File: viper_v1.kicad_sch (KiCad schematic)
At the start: 149 parts, among them J1 USB_B_Mini, J2 AVR-ISP-6, SW1 SW_RESET, SW10 KC_8, SW11 KC_9, SW12 KC_0, SW13 KC_MINS, SW14 KC_EQL, SW15 KC_BSPC, SW16 KC_TAB, SW17 KC_Q, SW18 KC_W, SW19 KC_E, SW2 KC_GRV, SW20 KC_R, SW21 KC_T, SW22 KC_Y, SW23 KC_U, SW24 KC_I, SW25 KC_O, SW26 KC_P, SW27 KC_LBRC, SW28 KC_RBRC, SW29 KC_BSLS, SW3 KC_1, SW30 KC_CAPS, SW31 KC_A, SW32 KC_S, SW33 KC_D, SW34 KC_F, SW35 KC_G, SW36 KC_H, SW37 KC_J, SW38 KC_K, SW39 KC_L, SW4 KC_2, SW40 KC_SCLN, SW41 KC_QUOT, SW42 KC_ENT, SW43 KC_LSFT, SW44 KC_Z, SW45 KC_X, SW46 KC_C, SW47 KC_V, SW48 KC_B, SW49 KC_N, SW5 KC_3, SW50 KC_M, SW51 KC_COMM, SW52 KC_DOT, SW53 KC_SLSH, SW54 KC_RSFT, SW55 KC_LEFT_GUI, SW56 KC_LEFT_ALT, SW57 KC_SPACE, SW58 KC_RIGHT_GUI, SW59 KC_RIGHT_ALT, SW6 KC_4, SW60 KC_BSPC, SW61 KC_BSPC, SW62 KC_BSPC, SW7 KC_5, SW8 KC_6, SW9 KC_7, U1 ATmega32U4-A, Y1 16MHz

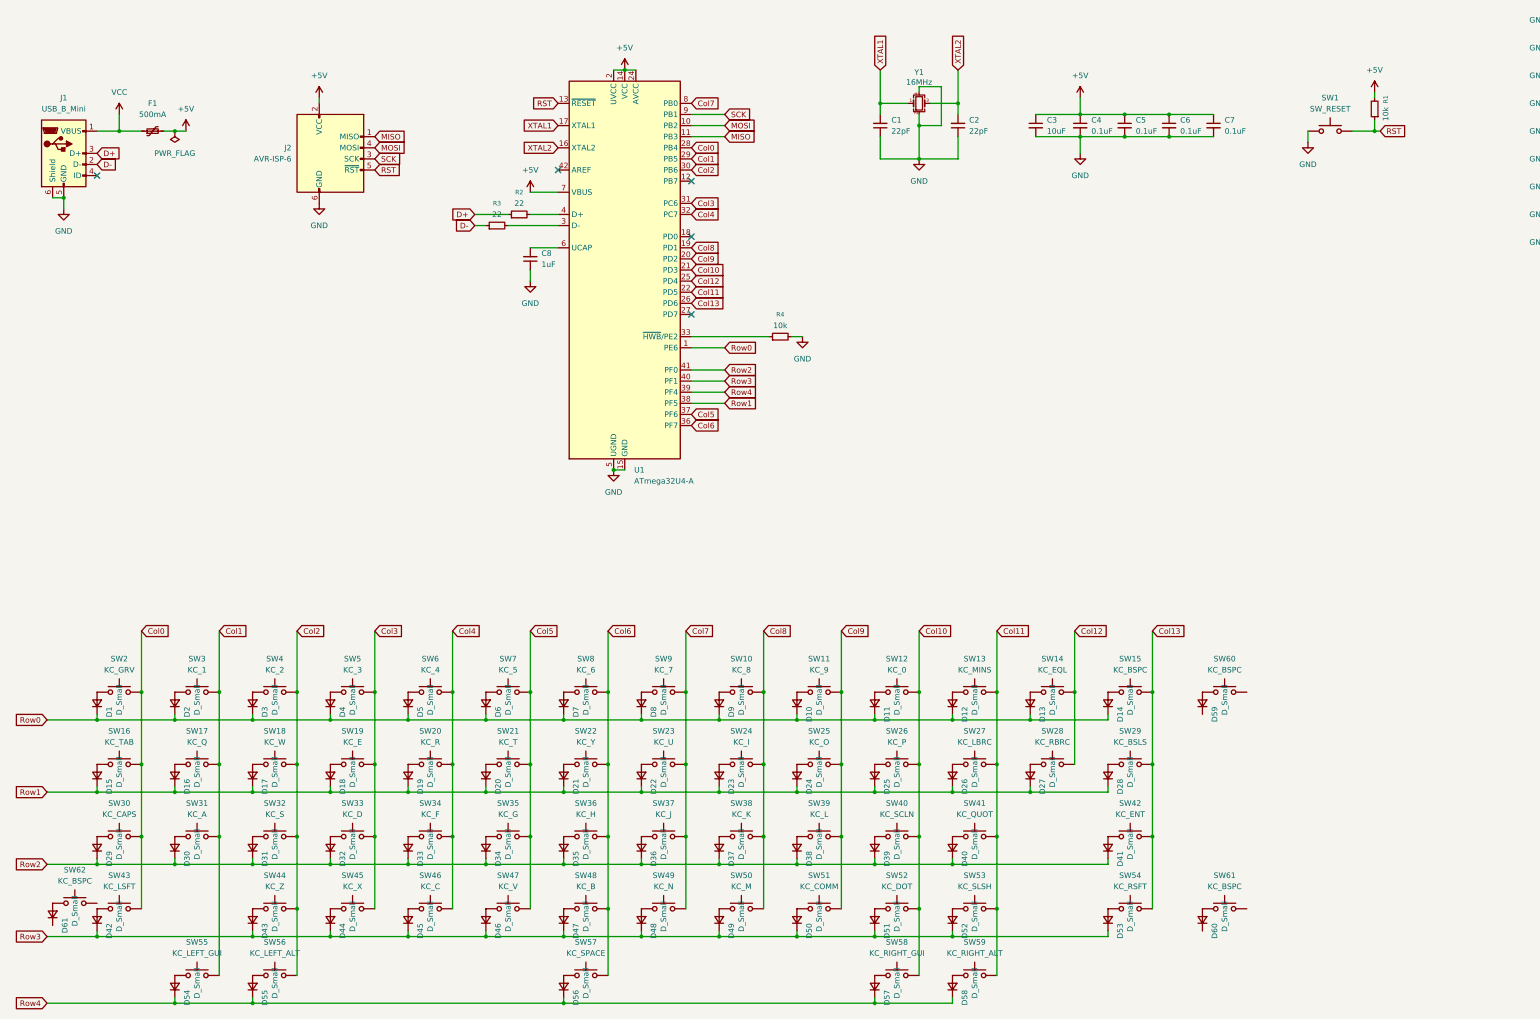
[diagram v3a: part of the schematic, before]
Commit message: Placed new footprints for iso enter, short shifts, stepped caps, fn & 2 more iso switches.
Added USBLC6-2SC6 for ESD protection
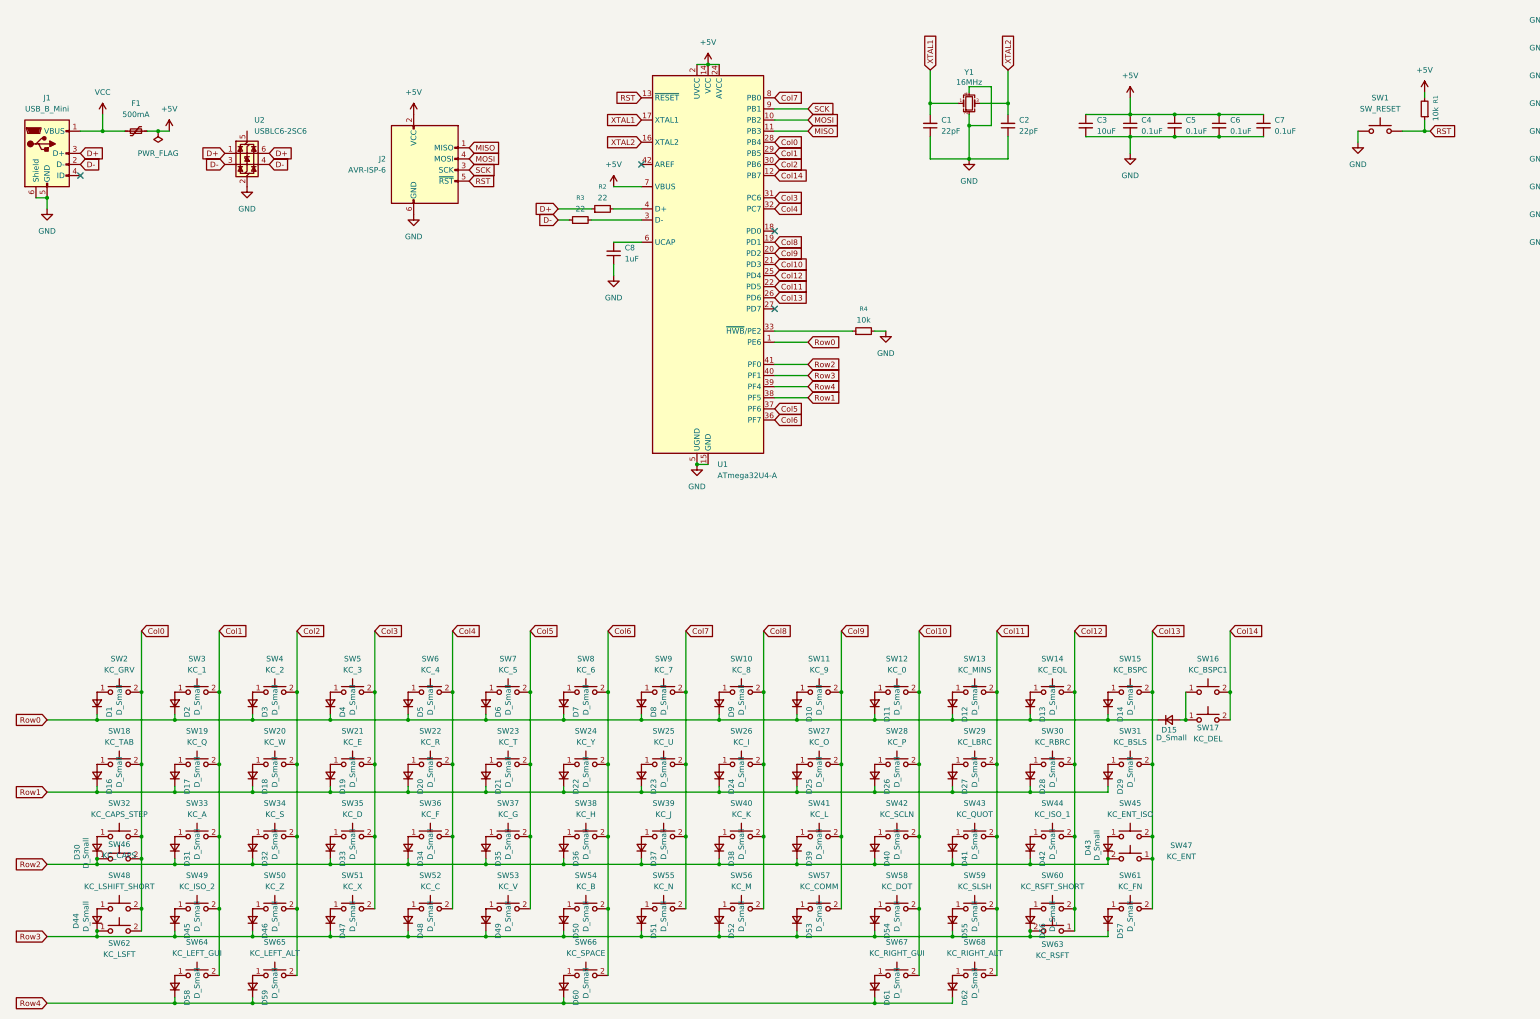
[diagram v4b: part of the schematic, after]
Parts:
- removed D60, D61: D_Small, Diode_SMD:D_SOD-123, symbol Device:D_Small
- added D42, D45, D56: D_Small, Diode_SMD:D_SOD-123, symbol Device:D_Small
- added SW44: KC_ISO_1, MX_Solderable:MX-Solderable-1U, symbol Switch:SW_Push
- added SW46: KC_CAPS, MX_Solderable:MX-Solderable-1.75U, symbol Switch:SW_Push
- added SW47: KC_ENT, MX_Solderable:MX-Solderable-2.25U-ReversedStabilizers, symbol Switch:SW_Push
- added SW49: KC_ISO_2, MX_Solderable:MX-Solderable-1U, symbol Switch:SW_Push
- added SW60: KC_RSFT_SHORT, MX_Solderable:MX-Solderable-1.75U, symbol Switch:SW_Push
- added SW63: KC_RSFT, MX_Solderable:MX-Solderable-2.75U-ReversedStabilizers, symbol Switch:SW_Push
- added U2: USBLC6-2SC6, Package_TO_SOT_SMD:SOT-23-6, symbol Power_Protection:USBLC6-2SC6
- SW16: renamed from SW60; value KC_BSPC -> KC_BSPC1; footprint MX_Solderable:MX-Solderable-2U -> MX_Solderable:MX-Solderable-1U
- SW17: renamed from SW61; value KC_BSPC -> KC_DEL; footprint MX_Solderable:MX-Solderable-2U -> MX_Solderable:MX-Solderable-1U
- SW32: renamed from SW30; value KC_CAPS -> KC_CAPS_STEP; footprint MX_Solderable:MX-Solderable-1.75U -> MX_Solderable:MX-Solderable-1.25U
- SW45: renamed from SW42; value KC_ENT -> KC_ENT_ISO; footprint MX_Solderable:MX-Solderable-2.25U-ReversedStabilizers -> MX_Solderable:MX-Solderable-2U-Vertical
- SW48: renamed from SW62; value KC_BSPC -> KC_LSHIFT_SHORT; footprint MX_Solderable:MX-Solderable-2U -> MX_Solderable:MX-Solderable-1.25U
- SW61: renamed from SW54; value KC_RSFT -> KC_FN; footprint MX_Solderable:MX-Solderable-2.75U-ReversedStabilizers -> MX_Solderable:MX-Solderable-1U
- renumbered D59 to D15, D15 to D16, D16 to D17, D17 to D18, D18 to D19, D19 to D20, D20 to D21, D21 to D22, D22 to D23, D23 to D24, D24 to D25, D25 to D26, D26 to D27, D27 to D28, D28 to D29, D29 to D30, D30 to D31, D31 to D32, D32 to D33, D33 to D34, D34 to D35, D35 to D36, D36 to D37, D37 to D38, D38 to D39, D39 to D40, D40 to D41, D41 to D43, D42 to D44, D43 to D46, D44 to D47, D45 to D48, D46 to D49, D47 to D50, D48 to D51, D49 to D52, D50 to D53, D51 to D54, D52 to D55, D53 to D57, D54 to D58, D55 to D59, D56 to D60, D57 to D61, D58 to D62, SW16 to SW18, SW17 to SW19, SW18 to SW20, SW19 to SW21, SW20 to SW22, SW21 to SW23, SW22 to SW24, SW23 to SW25, SW24 to SW26, SW25 to SW27, SW26 to SW28, SW27 to SW29, SW28 to SW30, SW29 to SW31, SW31 to SW33, SW32 to SW34, SW33 to SW35, SW34 to SW36, SW35 to SW37, SW36 to SW38, SW37 to SW39, SW38 to SW40, SW39 to SW41, SW40 to SW42, SW41 to SW43, SW44 to SW50, SW45 to SW51, SW46 to SW52, SW47 to SW53, SW48 to SW54, SW49 to SW55, SW50 to SW56, SW51 to SW57, SW52 to SW58, SW53 to SW59, SW43 to SW62, SW55 to SW64, SW56 to SW65, SW57 to SW66, SW58 to SW67, SW59 to SW68
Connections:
- net Col0: now also SW48.2, SW46.2
- net Col1: now also SW49.2
- net Col12: now also SW44.2, SW60.2, SW63.1
- net Col13: now also SW47.1
- net D+: now also U2.1 (I/O1), U2.6 (I/O1)
- net D-: now also U2.3 (I/O2), U2.4 (I/O2)
- net GND: now also U2.2 (GND)
- net Row0: now also D15.1 (K)
- net Row2: now also D42.1 (K), SW46.1, SW47.2
- net Row3: now also SW62.1, D45.1 (K), D56.1 (K), SW63.2
- net at SW48.1: now also D44.2 (A)
- net at D15.2 (A), SW16.1: now also SW17.1
- net Col14: now reaches SW17.2
- net Col14: now also SW16.2, U1.12 (PB7)
- new net: D42.2 (A), SW44.1
- new net: D56.2 (A), SW60.1
- new net: D45.2 (A), SW49.1
- no-connect marks 5 -> 4
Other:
- moved on the sheet: C1, C2, C3, C4, C5, C6, C7, C8, D15, F1, J1, J2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

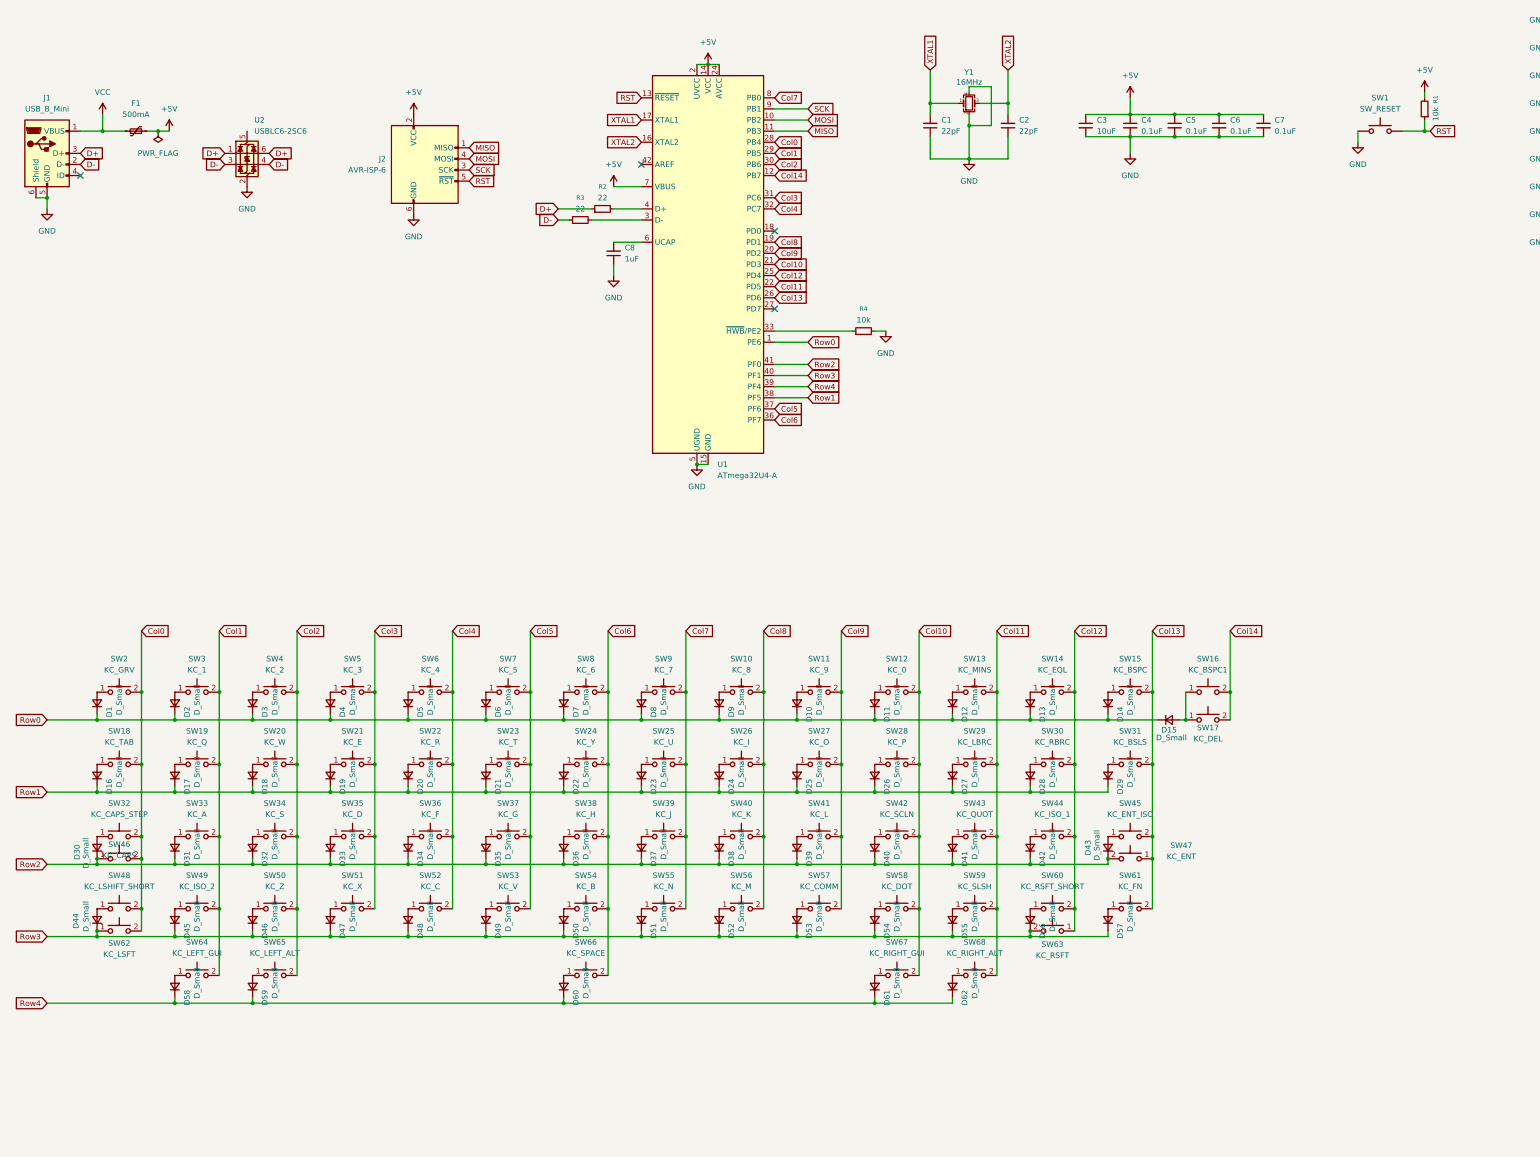
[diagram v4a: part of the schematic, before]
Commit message: Fixed broken cols for stacked keys & added HRO-U-M-M5DD-W-1.kicad_mod from mymakercorner/Phoenix_Project_No1
Set wider track width for power & default.

Moved parts around usb connector around

Started wiring usb.

Added GND zones
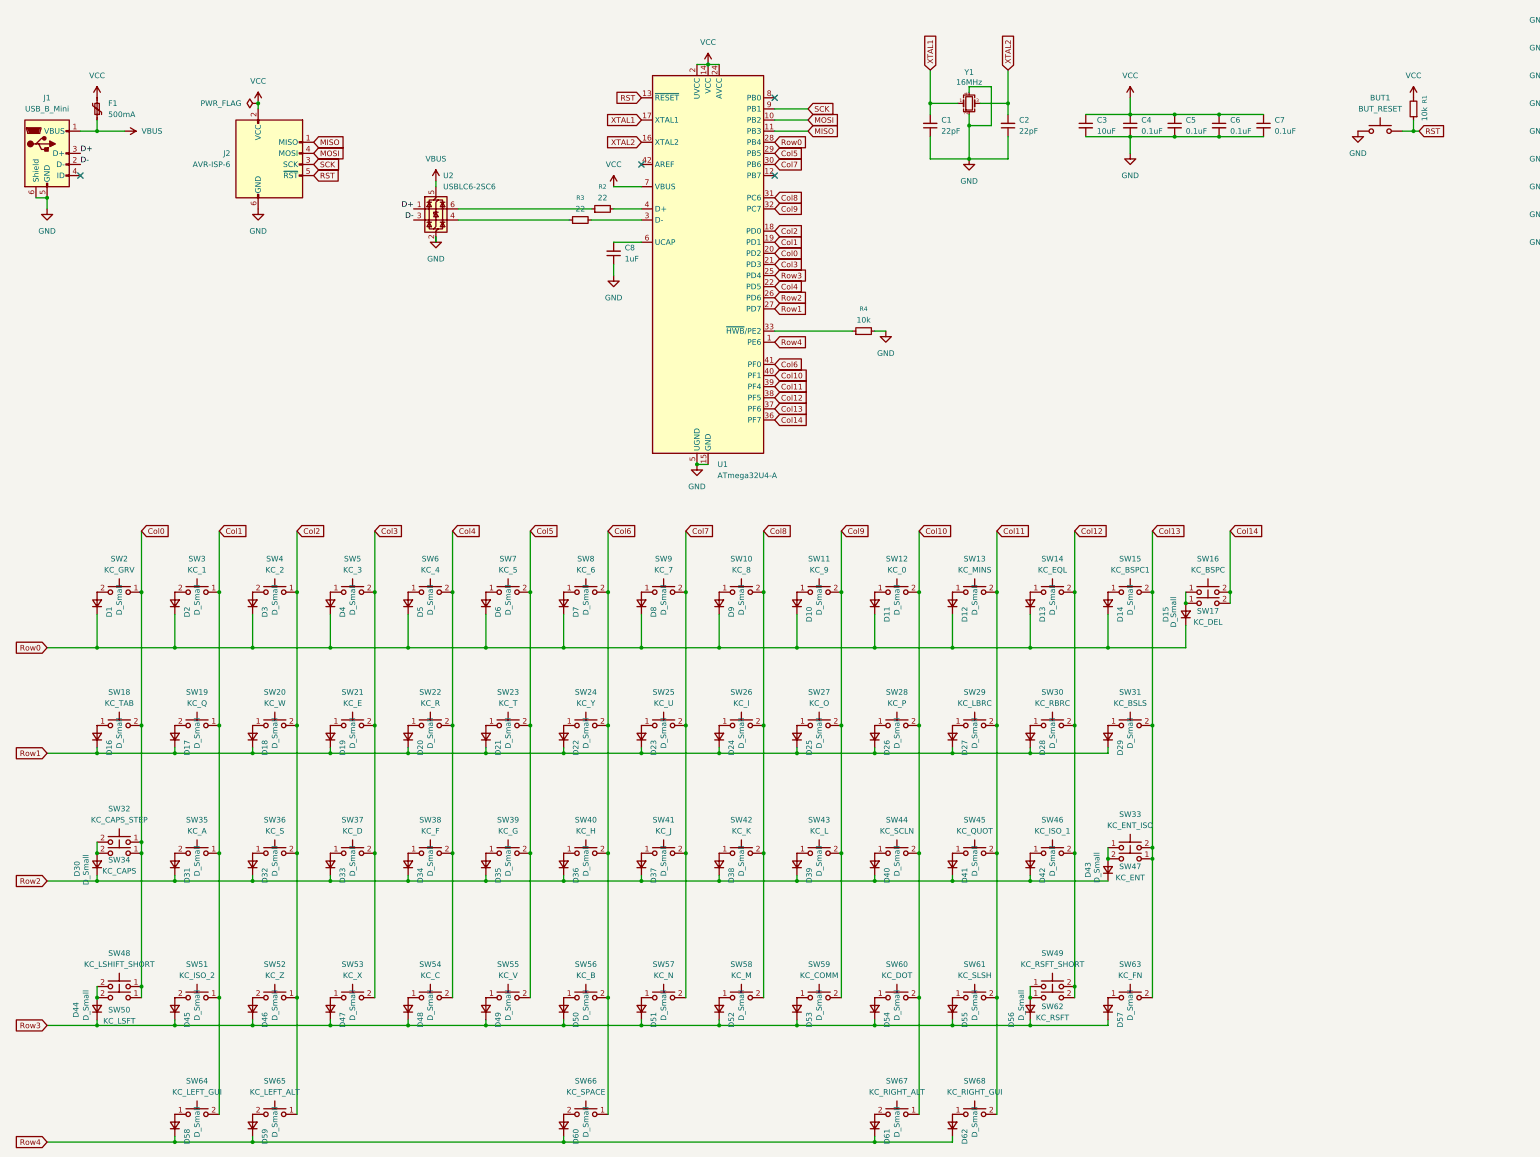
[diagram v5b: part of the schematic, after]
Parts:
- BUT1: renamed from SW1; value SW_RESET -> BUT_RESET; footprint random-keyboard-parts:SKQG-1155865 -> Button_Switch_SMD:SW_SPST_TL3342
- F1: footprint Fuse:Fuse_1206_3216Metric -> Fuse:Fuse_0805_2012Metric
- J1: footprint local:USB_miniB_hirose_5ST_hand -> local:HRO-U-M-M5DD-W-1
- SW67: value KC_RIGHT_GUI -> KC_RIGHT_ALT; footprint MX_Solderable:MX-Solderable-1U -> MX_Solderable:MX-Solderable-1.5U
- SW68: value KC_RIGHT_ALT -> KC_RIGHT_GUI; footprint MX_Solderable:MX-Solderable-1.5U -> MX_Solderable:MX-Solderable-1U
- renumbered SW16 to SW15, SW15 to SW16, SW45 to SW33, SW46 to SW34, SW33 to SW35, SW34 to SW36, SW35 to SW37, SW36 to SW38, SW37 to SW39, SW38 to SW40, SW39 to SW41, SW40 to SW42, SW41 to SW43, SW42 to SW44, SW43 to SW45, SW44 to SW46, SW60 to SW49, SW62 to SW50, SW49 to SW51, SW50 to SW52, SW51 to SW53, SW52 to SW54, SW53 to SW55, SW54 to SW56, SW55 to SW57, SW56 to SW58, SW57 to SW59, SW58 to SW60, SW59 to SW61, SW63 to SW62, SW61 to SW63
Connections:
- net +5V is gone; now on net VCC: C3.1, C4.1, C5.1, C6.1, C7.1, F1.2, J2.2 (VCC), R1.2, U1.14 (VCC), U1.2 (UVCC), U1.24 (AVCC), U1.34 (VCC), U1.44 (AVCC), U1.7 (VBUS)
- net Col0: now also SW2.1, SW32.1, SW34.1, SW48.1, SW50.1, U1.20 (PD2); no longer SW2.2, SW32.2, SW34.2, SW48.2, SW50.2, U1.28 (PB4)
- net Col1: now also SW19.1, SW3.1, SW35.1, SW51.1, U1.19 (PD1); no longer SW19.2, SW3.2, SW35.2, SW51.2, U1.29 (PB5)
- net Col10: now also SW67.1, U1.40 (PF1); no longer SW67.2, U1.21 (PD3)
- net Col11: now also U1.39 (PF4); no longer U1.22 (PD5)
- net Col12: now also SW62.2, U1.38 (PF5); no longer SW62.1, U1.25 (PD4)
- net Col13: now also SW15.2, U1.37 (PF6); no longer SW16.2, U1.26 (PD6)
- net Col14: now also SW16.2, U1.36 (PF7); no longer SW15.2, U1.12 (PB7)
- net Col2: now also SW4.1, SW52.1, SW65.1, U1.18 (PD0); no longer SW4.2, SW52.2, SW65.2, U1.30 (PB6)
- net Col3: now also U1.21 (PD3); no longer U1.31 (PC6)
- net Col4: now also U1.22 (PD5); no longer U1.32 (PC7)
- net Col5: now also U1.29 (PB5); no longer U1.37 (PF6)
- net Col6: now also SW66.1, U1.41 (PF0); no longer SW66.2, U1.36 (PF7)
- net Col7: now also U1.30 (PB6); no longer U1.8 (PB0)
- net Col8: now also U1.31 (PC6); no longer U1.19 (PD1)
- net Col9: now also U1.32 (PC7); no longer U1.20 (PD2)
- net D+: no longer R2.1, U2.6 (I/O1)
- net D-: no longer R3.1, U2.4 (I/O2)
- net Row0: now also U1.28 (PB4); no longer U1.1 (PE6)
- net Row1: now also U1.27 (PD7); no longer U1.38 (PF5)
- net Row2: now also U1.26 (PD6); no longer SW34.1, SW47.2, U1.41 (PF0)
- net Row3: now also U1.25 (PD4); no longer SW50.1, SW62.2, U1.40 (PF1)
- net Row4: now also U1.1 (PE6); no longer U1.39 (PF4)
- net VCC: no longer F1.1, J1.1 (VBUS)
- net at D46.2 (A): now also SW52.2; no longer SW52.1
- net at D14.2 (A): now also SW15.1; no longer SW16.1
- net at D30.2 (A): now also SW32.2, SW34.2; no longer SW32.1
- net at D44.2 (A): now also SW48.2, SW50.2; no longer SW48.1
- net at D61.2 (A): now also SW67.2; no longer SW67.1
- net at D31.2 (A): now also SW35.2; no longer SW35.1
- net VBUS: now reaches U2.5 (VBUS)
- net VBUS: now also F1.1, J1.1 (VBUS)
- net at D1.2 (A): now also SW2.2; no longer SW2.1
- net at D15.2 (A), SW17.1: now also SW16.1; no longer SW15.1
- net at D59.2 (A): now also SW65.2; no longer SW65.1
- net at D60.2 (A): now also SW66.2; no longer SW66.1
- net at D2.2 (A): now also SW3.2; no longer SW3.1
- net at D56.2 (A), SW49.1: now also SW62.1
- net at D45.2 (A): now also SW51.2; no longer SW51.1
- net at D17.2 (A): now also SW19.2; no longer SW19.1
- net at D43.2 (A), SW33.1: now also SW47.2
- net at D3.2 (A): now also SW4.2; no longer SW4.1
- new net: R3.1, U2.4 (I/O2)
- new net: R2.1, U2.6 (I/O1)
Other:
- moved on the sheet: D1, D10, D11, D12, D13, D14, D15, D16, D17, D18, D19, D2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

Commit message: Swapped ISP header & xtal footprint & connected all ratsnests
aligned vias

Renamed some screws & removed net labels
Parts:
- BUT1: value BUT_RESET -> BUT_RST
- D1, D10, D11, D12, D13, D14, D15, D16, D17, D18, D19, D2, D20, D21, D22, D23, D24, D25, D26, D27, D28, D29, D3, D30, D31, D32, D33, D34, D35, D36, D37, D38, D39, D4, D40, D41, D42, D43, D44, D45, D46, D47, D48, D49, D5, D50, D51, D52, D53, D54, D55, D56, D57, D58, D59, D6, D60, D61, D62, D7, D8, D9: footprint Diode_SMD:D_SOD-123 -> Diode_SMD:D_0805_2012Metric
- J2: value AVR-ISP-6 -> ISP; footprint random-keyboard-parts:Reset_Pretty-Mask -> local:isp_standard
- S1: value Screw_Terminal_01x01 -> Screw; footprint local:10x5_7x2.5mm -> local:5.5_5x2.5mm
- S2, S3, S4, S7: value Screw_Terminal_01x01 -> Screw
- S5, S6, S8, S9: value Screw_Terminal_01x01 -> Tofu Screw
- Y1: footprint Crystal:Crystal_SMD_3225-4Pin_3.2x2.5mm -> local:crystal_FA238-TSX3225; symbol Device:Crystal_GND24_Small -> Device:Crystal_GND3_Small
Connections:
- net Col2: now also SW65.2; no longer SW65.1
- net Col6: now also SW40.1; no longer SW40.2
- net GND: now also Y1.3; no longer Y1.2, Y1.4
- net XTAL2: now also Y1.2; no longer Y1.3
- net at D36.2 (A): now also SW40.2; no longer SW40.1
- net at D59.2 (A): now also SW65.1; no longer SW65.2
